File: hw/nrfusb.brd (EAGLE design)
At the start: 45 x 32 mm, 37 parts, among them J1 MF-CON-MICROUSB-RIGHT, J3 JST-ZH6SMT_VERT, M1 MOUNT, M2 MOUNT, M3 MOUNT, M4 MOUNT, U1 MF-REG-SOT235-3.3V-300mA, U2 USBLC6-2SC6, U3 TCAN334GSOT23, U4 TLP3317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

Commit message: Nominally complete board and schematic
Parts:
- removed R5: 100, mfpassives:R0805
- removed R6: 330, mfpassives:R0402
- removed U3: TCAN334GSOT23, fdcanusb:SOT23-8
- removed U4: TLP3317, fdcanusb:TLP3317
- added C12: 0.1uF, mfpassives:C0402
- C4: value 0.1uF -> 10uF; device mfpassives:C0402 -> mfpassives:C1206
- J2: device fdcanusb:F09H -> pinhead:2X04
- moved R1 13.3 mm to (27.8, 21.5), turned to 270 degrees
- moved J2 12.1 mm to (34.6, 4.10), turned to 180 degrees
- moved R2 11.9 mm to (26.2, 21.5), turned to 270 degrees
- moved D1 10.9 mm to (28.0, 18.5), turned to 270 degrees
- moved C4 9.08 mm to (26.4, 8.30), turned to 90 degrees
- moved D2 8.56 mm to (26.0, 18.5), turned to 270 degrees
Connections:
- removed net CAN_N: J2.2, U3.6, U4.4
- removed net CAN_P: J2.7, R5.P$1, U3.7
- removed net CAN_RX: U3.4, U5.26
- removed net CAN_SHDN: U3.5, U5.28
- removed net CAN_STB: U3.8, U5.25
- removed net CAN_TERM: U4.2, U5.29
- removed net CAN_TX: U3.1, U5.27
- removed net LED_CAN_RX: D2.ANODE, U5.41
- removed net LED_CAN_TX: D1.ANODE, U5.40
- removed net N$7: R5.P$2, U4.3
- removed net N$8: R6.P$2, U4.1
- new net LED_RF_RX: D2.ANODE, U5.29
- new net LED_RF_TX: D1.ANODE, U5.28
- new net NRF_CE: J2.6, U5.39
- new net NRF_CS: J2.5, U5.43
- new net NRF_IRQ: J2.1, U5.44
- new net NRF_MISO: J2.2, U5.41
- new net NRF_MOSI: J2.3, U5.42
- new net NRF_SCK: J2.4, U5.40
- net +3V3: now also C12.P$1, J2.7; no longer R6.P$1, U3.3
- net GND: now also C12.P$2, J2.8; no longer J2.3, J2.5, J2.6, U3.2
- net LED_COM: now also U5.27; no longer U5.43
- net LED_PWR: now also U5.26; no longer U5.42
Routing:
- net NRF_SCK: track 0.00 -> 38.2 mm, vias 0 -> 1
- net LED_RF_RX: track 0.00 -> 37.0 mm
- net NRF_MISO: track 0.00 -> 36.3 mm, vias 0 -> 1
- net CAN_TERM: track 34.5 -> 0.00 mm
- net NRF_CE: track 0.00 -> 33.1 mm, vias 0 -> 1
- net NRF_IRQ: track 0.00 -> 29.6 mm, vias 0 -> 1
- net NRF_MOSI: track 0.00 -> 29.4 mm, vias 0 -> 2
- net NRF_CS: track 0.00 -> 26.3 mm, vias 0 -> 1
- net LED_CAN_TX: track 17.6 -> 0.00 mm, vias 2 -> 0
- net LED_CAN_RX: track 14.1 -> 0.00 mm, vias 2 -> 0
- net CAN_P: track 13.5 -> 0.00 mm
- net CAN_SHDN: track 10.6 -> 0.00 mm, vias 2 -> 0
- net LED_RF_TX: track 0.00 -> 10.6 mm, vias 0 -> 2
- net CAN_N: track 9.92 -> 0.00 mm
- net CAN_RX: track 9.07 -> 0.00 mm, vias 2 -> 0
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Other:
- board text added: "nrfusb r1 (c) jjp@pobox.com 2019"
- board text removed: "CAN"
- board text removed: "fdcanusb r1 (c) jjp@pobox.com 2019"

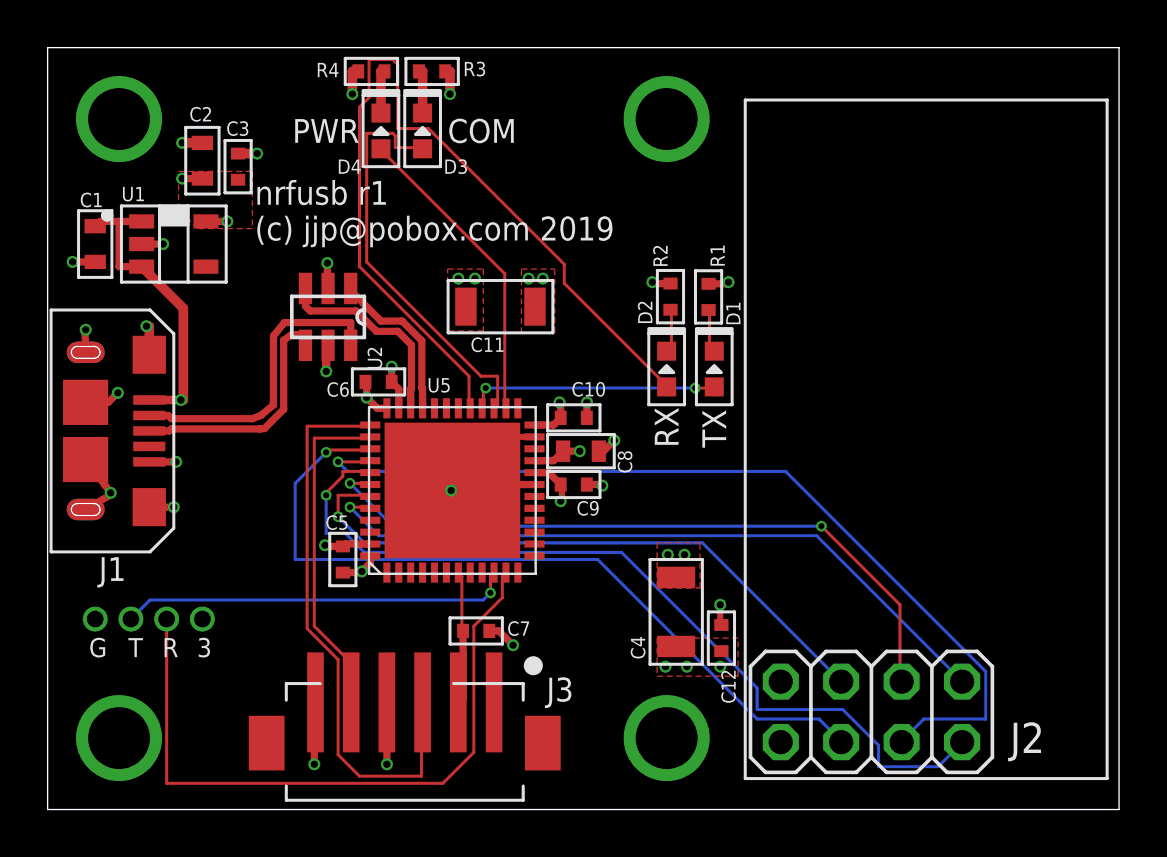
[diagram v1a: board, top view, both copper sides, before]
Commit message: Update with correct stm32 pinout
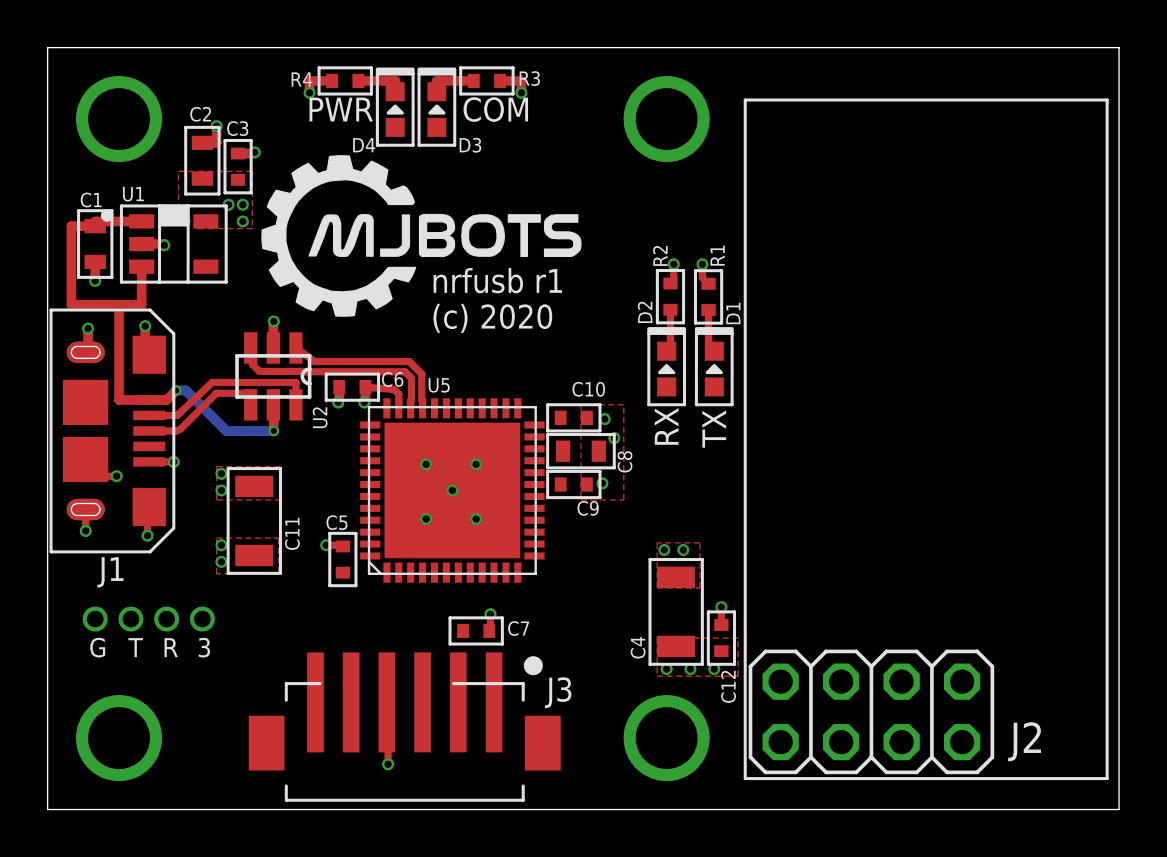
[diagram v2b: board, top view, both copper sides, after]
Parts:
- U5: device fdcanusb:QFN50P700X700X60-49N -> nrfusb:QFN50P700X700X60-49N
- moved C11 13.7 mm to (8.68, 12.1), turned to 270 degrees
- moved U2 3.40 mm to (9.48, 18.2)
- moved R3 2.33 mm to (18.4, 30.6)
- moved R4 1.17 mm to (12.5, 30.6)
- moved C6 1.12 mm to (12.8, 17.7), turned to 180 degrees
- moved D3 1.08 mm to (16.4, 29.4)
- moved D4 1.08 mm to (14.6, 29.4)
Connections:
- net +3V3: now also U5.1, U5.23, U5.35; no longer U5.24, U5.36
- net GND: no longer U5.19, U5.23, U5.35, U5.47
- net LED_PWR: now also U5.28; no longer U5.26
- net LED_RF_RX: now also U5.26; no longer U5.29
- net LED_RF_TX: now also U5.25; no longer U5.28
- net NRF_CE: now also U5.17; no longer U5.39
- net NRF_CS: now also U5.12; no longer U5.43
- net NRF_IRQ: now also U5.18; no longer U5.44
- net NRF_MISO: now also U5.14; no longer U5.41
- net NRF_MOSI: now also U5.15; no longer U5.42
- net NRF_SCK: now also U5.13; no longer U5.40
- net SWCLK: now also U5.37; no longer U5.38
- net SWDIO: now also U5.36; no longer U5.37
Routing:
- net NRF_SCK: track 38.2 -> 0.00 mm, vias 1 -> 0
- net LED_RF_RX: track 37.0 -> 0.00 mm
- net NRF_MISO: track 36.3 -> 0.00 mm, vias 1 -> 0
- net NRF_CE: track 33.1 -> 0.00 mm, vias 1 -> 0
- net NRF_IRQ: track 29.6 -> 0.00 mm, vias 1 -> 0
- net NRF_MOSI: track 29.4 -> 0.00 mm, vias 2 -> 0
- net DEBUG_RX: track 28.4 -> 0.00 mm
- net NRF_CS: track 26.3 -> 0.00 mm, vias 1 -> 0
- net SWDIO: track 24.0 -> 0.00 mm
- net LED_COM: track 17.2 -> 0.00 mm
- net DEBUG_TX: track 16.5 -> 0.00 mm, vias 1 -> 0
- net SWCLK: track 14.1 -> 0.00 mm
- net GND: track 36.4 -> 22.4 mm, vias 28 -> 32
- net LED_PWR: track 13.1 -> 0.00 mm
- net +3V3: track 14.5 -> 2.84 mm, vias 13 -> 9
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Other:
- board text added: "nrfusb r1 (c) 2020"
- board text removed: "nrfusb r1 (c) jjp@pobox.com 2019"

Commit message: Auto-route
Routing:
- net DEBUG_RX: track 0.00 -> 29.4 mm
- net NRF_IRQ: track 0.00 -> 24.9 mm
- net SWDIO: track 0.00 -> 24.8 mm
- net NRF_SCK: track 0.00 -> 24.2 mm
- net NRF_MISO: track 0.00 -> 23.9 mm
- net NRF_CE: track 0.00 -> 23.5 mm, vias 0 -> 1
- net NRF_MOSI: track 0.00 -> 18.0 mm, vias 0 -> 1
- net DEBUG_TX: track 0.00 -> 17.1 mm, vias 0 -> 1
- net NRF_CS: track 0.00 -> 15.5 mm, vias 0 -> 1
- net LED_PWR: track 0.00 -> 13.3 mm
- net LED_COM: track 0.00 -> 12.8 mm
- net SWCLK: track 0.00 -> 12.5 mm, vias 0 -> 2
- net +3V3: track 2.84 -> 12.8 mm, vias 9 -> 14
- net LED_RF_TX: track 0.00 -> 9.06 mm, vias 0 -> 2
- net LED_RF_RX: track 0.00 -> 8.29 mm
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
